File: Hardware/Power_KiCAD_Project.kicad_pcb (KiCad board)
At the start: 4 copper layers, 80 x 93.2 mm, 83 parts, among them J1 Barrel_Jack_MountingPin, J2 XT60 Cell 5, J3 XT60 Cell 4, J4 XT60 Cell 3, J5 XT60 Cell 2, J6 XT60 Cell 1, J7 XT60 To External Switch, J8 L717SDC37P1ACH4F, Q1 PSMN2R6-40YS, Q2 BSS84PH6327XTSA2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

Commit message: Added design rules for JLCPCB
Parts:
- moved R19 193.4 mm to (265.0, 30.6), turned to 0 degrees
- moved R18 183.4 mm to (260.6, 35.6), turned to 0 degrees
- moved R16 180.4 mm to (269.3, 25.3), turned to 0 degrees
- moved D5 173.0 mm to (269.2, 32.8)
- moved C34 170.8 mm to (265.1, 22.8), turned to 0 degrees
- moved R17 169.7 mm to (260.6, 33.1), turned to 0 degrees
- moved D6 167.4 mm to (264.9, 38.2)
- moved C36 164.2 mm to (279.6, 22.8), turned to 0 degrees
- moved C30 160.0 mm to (260.6, 30.6), turned to 0 degrees
- moved C1 155.2 mm to (264.4, 45.1), turned to 0 degrees
- moved C29 155.2 mm to (265.0, 28.1), turned to 0 degrees
- moved C31 155.0 mm to (269.4, 22.8)
- moved C32 152.7 mm to (265.0, 25.6), turned to 0 degrees
- moved C35 152.1 mm to (260.6, 25.6), turned to 0 degrees
- moved C28 149.2 mm to (269.3, 27.8), turned to 0 degrees
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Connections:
- C3 pad 1: /PACK_M5 -> /Buck_Converters/V_IN
- C36 pad 1: /DSUB-37_Bus/NRST -> GND
- C36 pad 2: GND -> /DSUB-37_Bus/NRST
- C4 pad 1: /PACK_M5 -> /Buck_Converters/V_IN
- C5 pad 1: /PACK_M5 -> /Buck_Converters/V_IN
- C6 pad 1: /PACK_M5 -> /Buck_Converters/V_IN
- J1 pad 1: /PACK_M5 -> /Buck_Converters/V_IN
- J1 pad 2: /LiPo Pack Monitor/PACK- -> GNDREF
- J7 pad 1: GNDREF -> /Buck_Converters/V_IN
- J7 pad 2: Net-(J7-Pad2) -> /PACK_M5
- Q3 pad 1: /LiPo Pack Monitor/PACK- -> GNDREF
- Q3 pad 2: /LiPo Pack Monitor/PACK- -> GNDREF
- Q3 pad 3: /LiPo Pack Monitor/PACK- -> GNDREF
- R10 pad 1: Net-(J7-Pad2) -> GNDREF
- R15 pad 2: /LiPo Pack Monitor/PACK- -> GNDREF
- R8 pad 2: Net-(J7-Pad2) -> GNDREF
- U3 pad 2: /PACK_M5 -> /Buck_Converters/V_IN
- U4 pad 2: /PACK_M5 -> /Buck_Converters/V_IN
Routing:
- net +3V3: track 305.7 -> 0.00 mm, vias 21 -> 0
- net /PACK_M5: track 213.0 -> 0.00 mm, vias 20 -> 0
- net +5V: track 149.7 -> 0.00 mm, vias 7 -> 0
- net /DSUB-37_Bus/Alert_scl: track 135.1 -> 0.00 mm, vias 3 -> 0
- net /STM32L562VET6Q 1/DEBUG_SWDIO: track 132.9 -> 0.00 mm, vias 2 -> 0
- net /STM32L562VET6Q 1/DEBUG_SWCLK: track 129.8 -> 0.00 mm, vias 2 -> 0
- net /DSUB-37_Bus/Alert_sda: track 129.3 -> 0.00 mm, vias 3 -> 0
- net /DSUB-37_Bus/Alert_Active: track 125.4 -> 0.00 mm, vias 2 -> 0
- net /DSUB-37_Bus/NRST: track 119.8 -> 0.00 mm, vias 4 -> 0
- net /LiPo Pack Monitor/PACK-: track 82.5 -> 0.00 mm, vias 3 -> 0
- net Net-(C7-Pad2): track 69.5 -> 0.00 mm, vias 3 -> 0
- net Net-(C8-Pad2): track 67.4 -> 0.00 mm
- net /BATT_ALERT: track 67.3 -> 0.00 mm, vias 6 -> 0
- net /I2C_SDA: track 59.8 -> 0.00 mm, vias 2 -> 0
- net /I2C_SCL: track 57.7 -> 0.00 mm, vias 2 -> 0
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- removed copper zone on 3.3V.Cu, net +3V3
- removed copper zone on GND.Cu, net GND
- removed copper zone on GND.Cu, net GNDREF
- removed copper zone on GND.Cu, net Net-(J7-Pad2)
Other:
- net class DIFF_90_USB removed
- net class Default: clearance 0.05 -> 0.5; trace_width 0.25 -> 0.2
- net class Mostly Safe Minimums added: clearance 0.127, trace_width 0.127, via_dia 0.45, via_drill 0.3
- net class Trace Minimums added: clearance 0.2, trace_width 0.15, via_dia 0.8, via_drill 0.4
- net class Trace to Trace Abs. Minimums added: clearance 0.09, trace_width 0.09, via_dia 0.8, via_drill 0.4
- net class Via Different Net Minimums added: clearance 0.5, trace_width 0.15, via_dia 0.4, via_drill 0.2
- net class Via Same Net Minimums added: clearance 0.254, trace_width 0.2, via_dia 0.4, via_drill 0.2
- rule trace_clearance: 0.05 -> 0.5

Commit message: Routed GNDREF side of board
Correcting keepout silkscreen added 3mm to top and bottom, much appreciated!
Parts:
- C11, C12, C13, C14, C15, C16, C19, C22, C23: footprint Capacitor_SMD:C_0603_1608Metric_Pad1.08x0.95mm_HandSolder -> Capacitor_SMD:C_1206_3216Metric_Pad1.42x1.75mm_HandSolder
- C18, C20, C21: footprint Capacitor_SMD:C_0603_1608Metric_Pad1.08x0.95mm_HandSolder -> Resistor_SMD:R_0603_1608Metric_Pad1.05x0.95mm_HandSolder
- R1, R2, R3, R4, R5, R6, R9: footprint Resistor_SMD:R_0603_1608Metric_Pad1.05x0.95mm_HandSolder -> Resistor_SMD:R_1206_3216Metric_Pad1.42x1.75mm_HandSolder
- moved U6 168.5 mm to (104.6, 117.2), turned to 180 degrees
- moved RV1 123.4 mm to (57.0, 83.8), turned to 315 degrees
- moved C20 111.4 mm to (97.1, 76.5)
- moved C16 109.8 mm to (98.8, 73.2), turned to 270 degrees
- moved R14 109.4 mm to (101.8, 93.3), turned to 270 degrees
- moved R9 104.9 mm to (106.6, 79.2), turned to 180 degrees
- moved C3 104.9 mm to (209.5, 132.0)
- moved U3 104.5 mm to (190.8, 131.9), turned to 90 degrees
- moved C10 101.8 mm to (223.2, 128.6)
- moved R6 100.3 mm to (101.2, 73.2), turned to 270 degrees
- moved R11 98.9 mm to (107.3, 87.4)
- moved U5 98.8 mm to (100.1, 82.0), turned to 90 degrees
- moved C22 96.6 mm to (107.8, 82.8), turned to 90 degrees
- moved R5 96.3 mm to (106.2, 73.2), turned to 270 degrees
- moved C7 94.7 mm to (194.6, 145.0)
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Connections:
- J1 pad 2: GNDREF -> GND
- J1 pad 3: (no net) -> GND
- Q3 pad 1: GNDREF -> GND
- Q3 pad 2: GNDREF -> GND
- Q3 pad 3: GNDREF -> GND
- R15 pad 2: GNDREF -> GND
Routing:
- net GNDREF: track 0.00 -> 212.6 mm, vias 0 -> 45
- net /PACK_M5: track 0.00 -> 71.9 mm
- net GND: track 0.00 -> 55.3 mm, vias 0 -> 14
- net /LiPo Pack Monitor/VC5: track 0.00 -> 52.4 mm
- net /LiPo Pack Monitor/VC4: track 0.00 -> 45.2 mm
- net Net-(Q1-Pad1): track 0.00 -> 43.0 mm
- net /LiPo Pack Monitor/VC3: track 0.00 -> 36.3 mm
- net Net-(C18-Pad1): track 0.00 -> 32.4 mm, vias 0 -> 2
- net /PACK_M2: track 0.00 -> 32.2 mm
- net /PACK_M4: track 0.00 -> 32.0 mm
- net /LiPo Pack Monitor/VC2: track 0.00 -> 25.9 mm
- net /PACK_M3: track 0.00 -> 24.4 mm
- net /PACK_M1: track 0.00 -> 20.8 mm
- net /LiPo Pack Monitor/VC1: track 0.00 -> 14.8 mm
- net Net-(Q1-Pad4): track 0.00 -> 11.2 mm, vias 0 -> 3
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- added copper zone on GND.Cu, net GND
- added copper zone on GND.Cu, net GNDREF

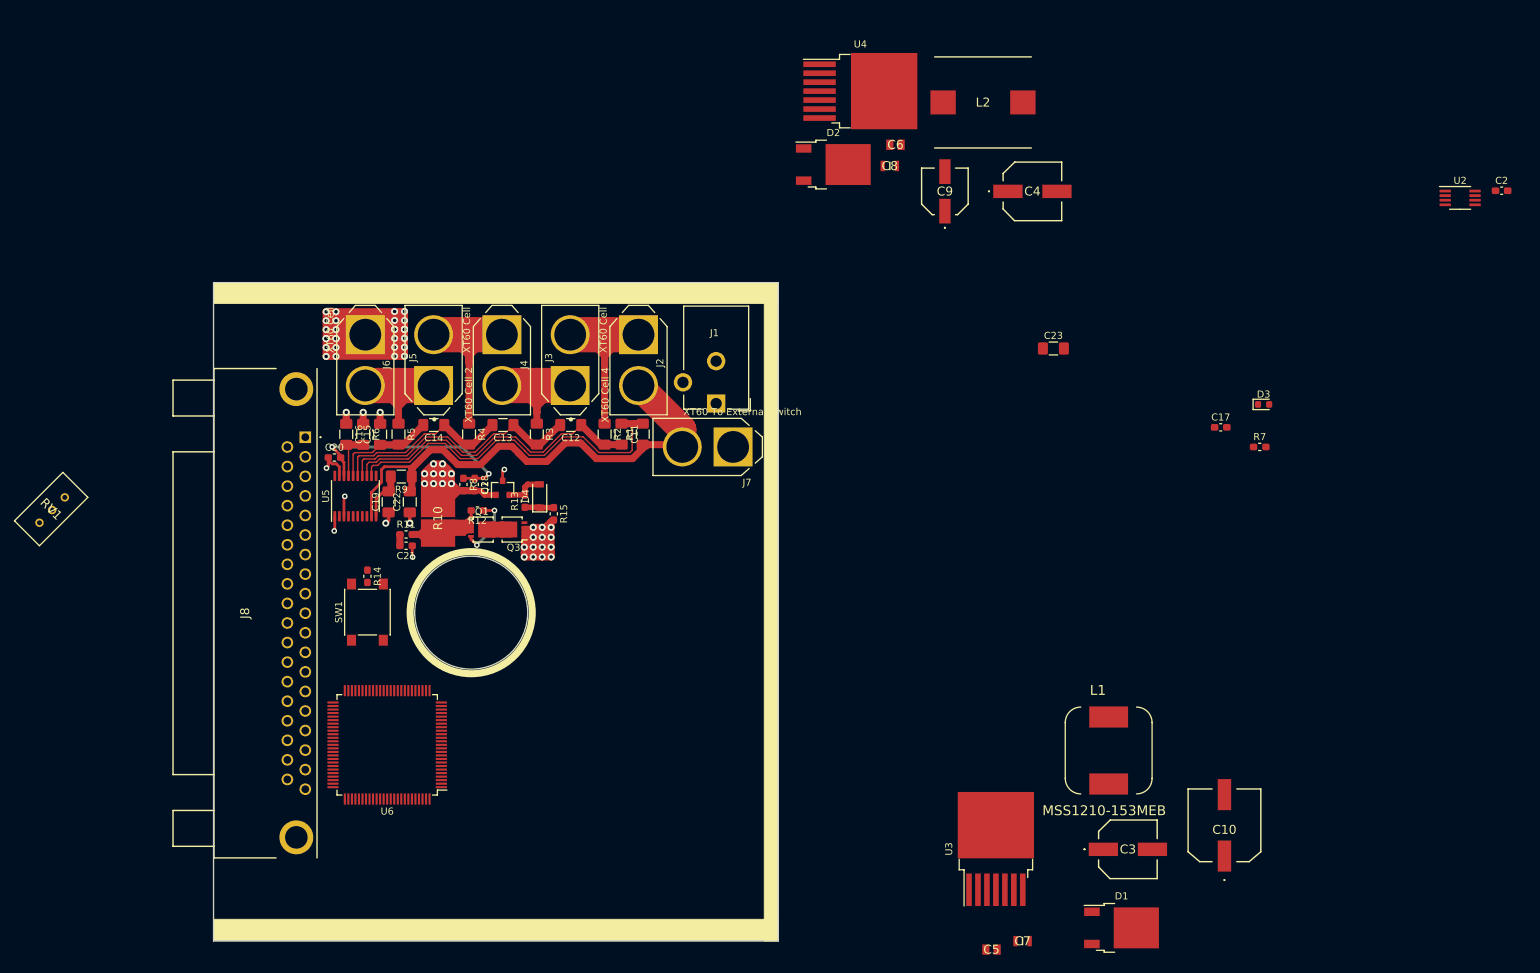
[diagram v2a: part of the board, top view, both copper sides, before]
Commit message: Routed 3v3 and 5v buck converters
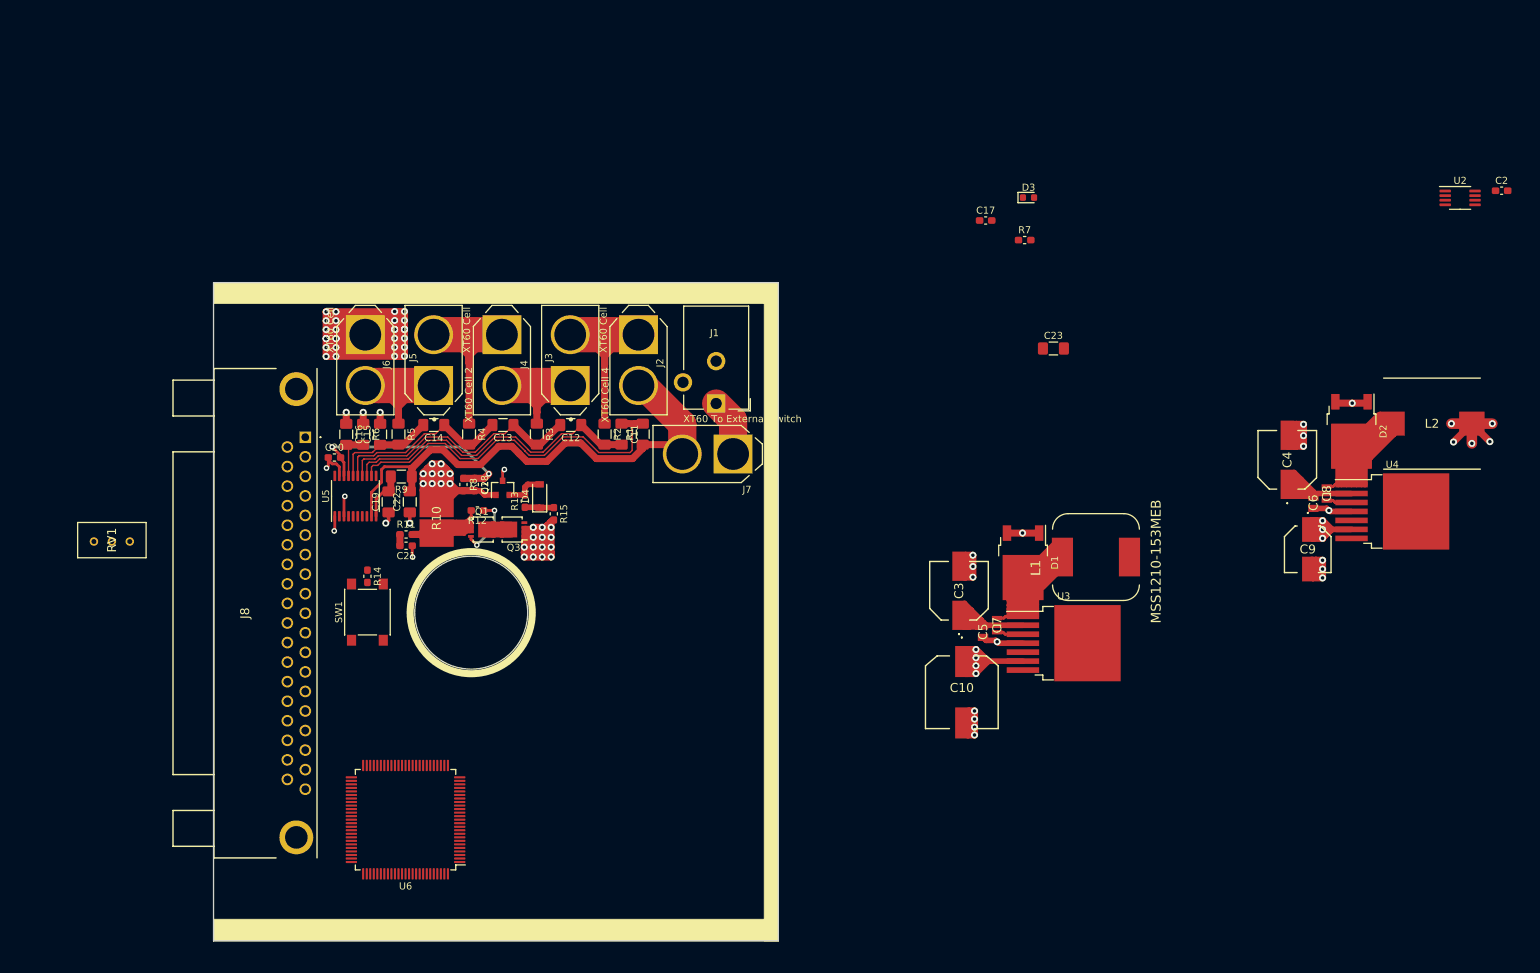
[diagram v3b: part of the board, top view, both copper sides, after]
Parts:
- moved U4 96.0 mm to (247.0, 84.1)
- moved D2 82.6 mm to (241.2, 72.8), turned to 270 degrees
- moved L2 78.2 mm to (252.6, 71.7)
- moved C6 77.9 mm to (235.8, 82.9), turned to 270 degrees
- moved C8 77.4 mm to (237.7, 81.6), turned to 90 degrees
- moved C9 72.2 mm to (235.0, 89.5), turned to 180 degrees
- moved D1 53.6 mm to (194.7, 91.4), turned to 270 degrees
- moved C4 52.4 mm to (232.1, 76.8), turned to 90 degrees
- moved C5 45.0 mm to (189.0, 101.2), turned to 270 degrees
- moved C7 44.9 mm to (191.0, 100.2), turned to 90 degrees
- moved C17 44.4 mm to (189.4, 42.9)
- moved D3 44.4 mm to (195.4, 39.7)
- moved R7 44.4 mm to (194.9, 45.7)
- moved C3 43.7 mm to (185.6, 95.4), turned to 90 degrees
- moved C10 41.7 mm to (186.0, 109.8), turned to 180 degrees
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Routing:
- net /Buck_Converters/V_IN: track 0.00 -> 65.9 mm
- net Net-(C7-Pad2): track 0.00 -> 63.1 mm
- net GND: track 55.3 -> 117.0 mm, vias 14 -> 31
- net Net-(C8-Pad2): track 0.00 -> 58.1 mm
- net +3V3: track 0.00 -> 34.9 mm, vias 0 -> 8
- net +5V: track 0.00 -> 26.4 mm, vias 0 -> 4
- net Net-(C7-Pad1): track 0.00 -> 3.77 mm
- net Net-(C8-Pad1): track 0.00 -> 3.61 mm
- net /PACK_M5: track 71.9 -> 74.2 mm
- added copper zone on 3.3V.Cu, net +3V3

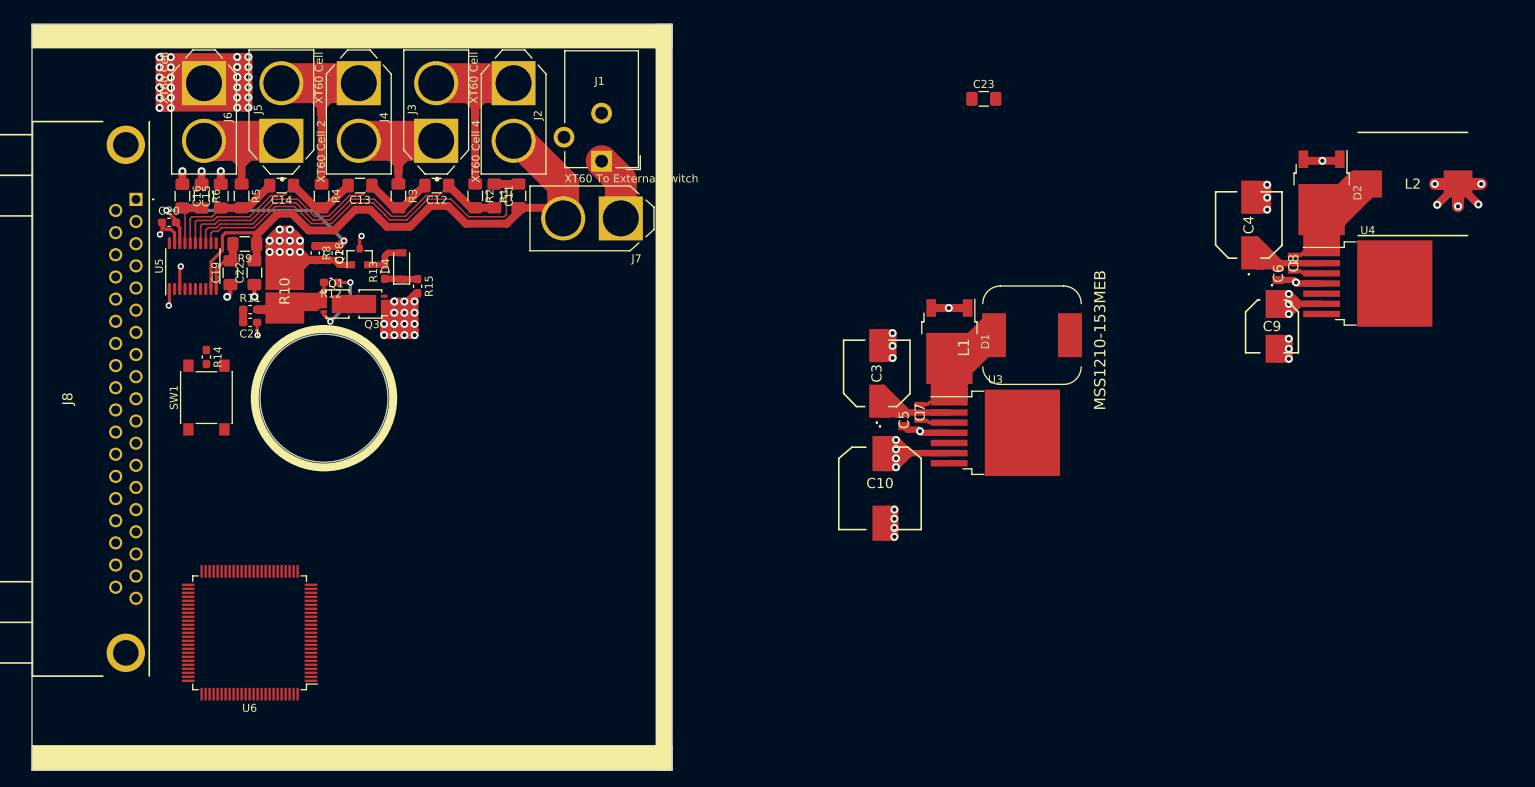
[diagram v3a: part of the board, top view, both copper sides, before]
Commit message: Routed most internal power/ground planes
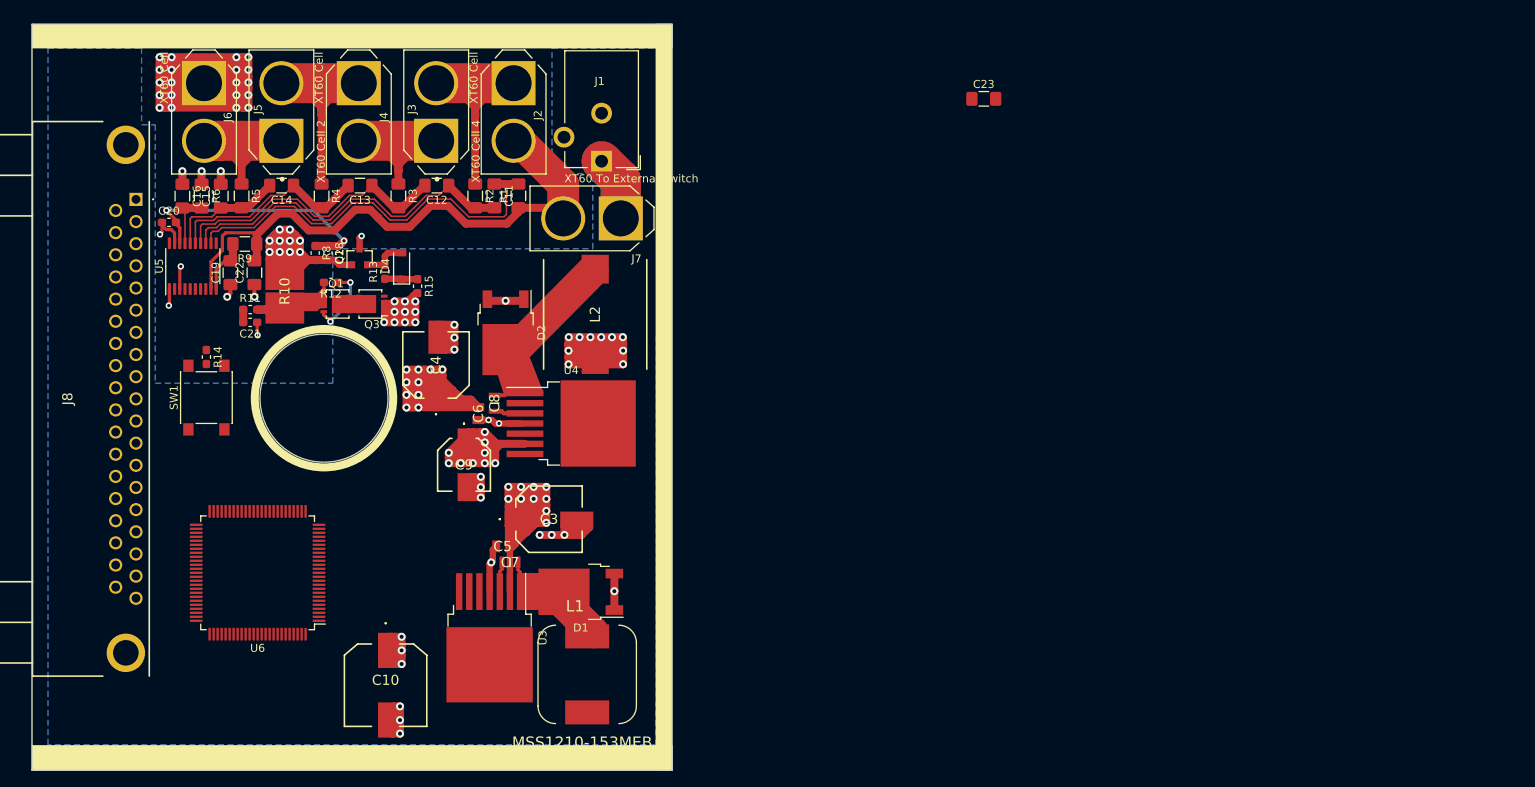
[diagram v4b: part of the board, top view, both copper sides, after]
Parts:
- moved L2 103.5 mm to (150.4, 88.0), turned to 270 degrees
- moved D2 103.5 mm to (139.2, 90.3)
- moved C4 103.1 mm to (130.5, 94.3)
- moved C9 102.5 mm to (134.0, 106.8)
- moved C6 101.5 mm to (135.8, 100.4)
- moved C8 101.4 mm to (137.8, 99.1)
- moved U4 101.1 mm to (147.4, 101.6)
- moved L1 69.9 mm to (149.4, 133.0), turned to 0 degrees
- moved U3 68.2 mm to (137.2, 128.4), turned to 270 degrees
- moved C10 66.5 mm to (124.2, 134.3)
- moved D1 55.7 mm to (148.6, 122.7), turned to 180 degrees
- moved C7 54.6 mm to (139.8, 119.0), turned to 0 degrees
- moved C5 52.6 mm to (138.8, 117.0), turned to 180 degrees
- moved C3 44.8 mm to (144.6, 113.6), turned to 0 degrees
- moved U6 7.57 mm to (108.2, 120.3)
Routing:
- net /Buck_Converters/V_IN: track 65.9 -> 169.0 mm, vias 0 -> 20
- net +3V3: track 34.9 -> 87.0 mm, vias 8 -> 19
- net Net-(C7-Pad2): track 63.1 -> 39.8 mm
- net GND: track 117.0 -> 102.9 mm, vias 31 -> 27
- net +5V: track 26.4 -> 15.3 mm, vias 4 -> 3
- net Net-(C8-Pad2): track 58.1 -> 56.2 mm
- net GNDREF: track 212.6 -> 211.8 mm, vias 45 -> 37
- added copper zone on 3.3V.Cu, net /Buck_Converters/V_IN
- added copper zone on B.Cu, net GND
